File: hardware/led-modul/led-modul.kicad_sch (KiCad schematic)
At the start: 123 parts, among them J201 24V IN 20A, J202 BLOKK 1, J203 BLOKK 2, J204 BLOKK 3, Q201 NTMFS5C604NL, Q202 NTD5C648NL, Q203 NTD5C648NL, Q204 NTD5C648NL, Q205 NTD5C648NL, Q206 NTD5C648NL, Q207 NTD5C648NL, U201 UCC27524DR, U202 UCC27524DR, U203 UCC27524DR, U204 LM74700-Q1, U205 MC78L12ACDR2G, U206 INA181A2IDBVR

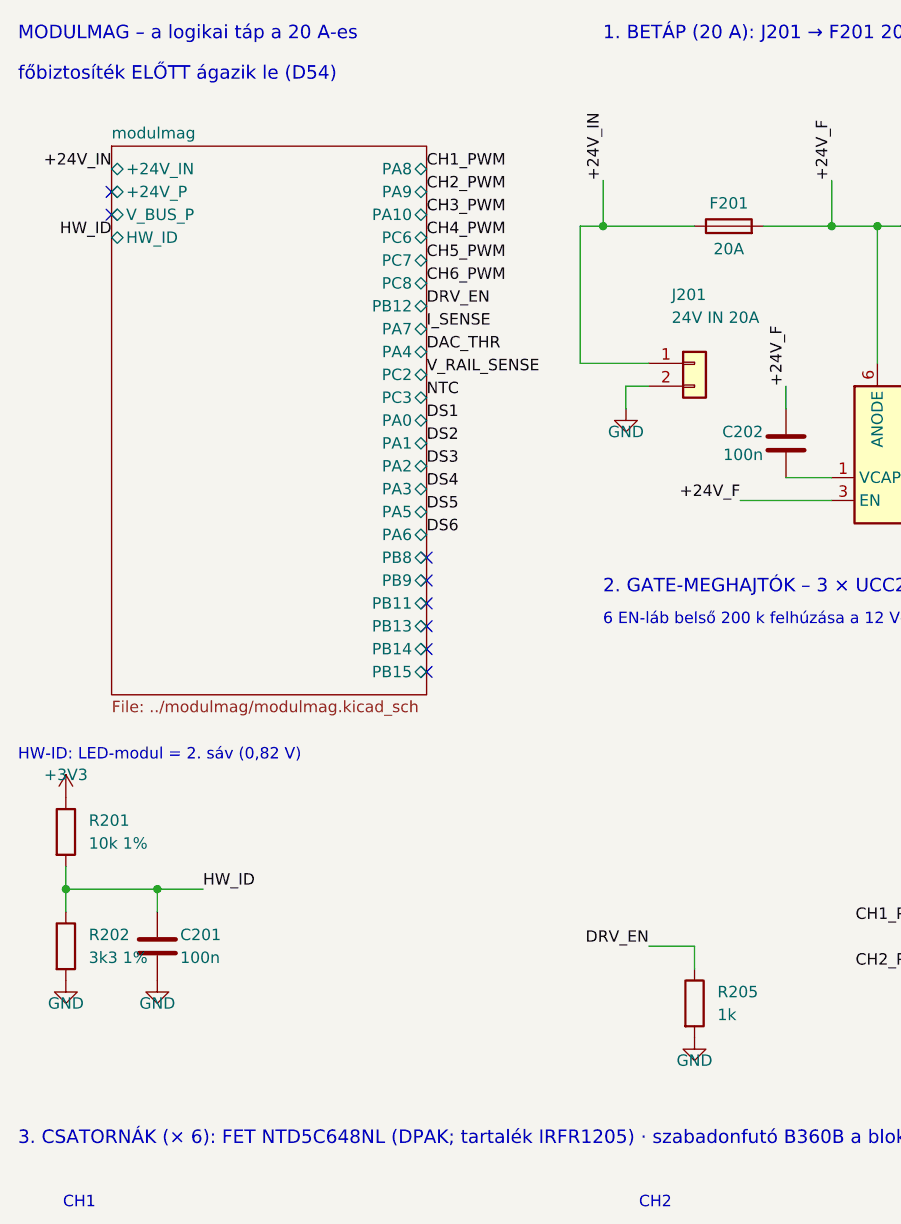
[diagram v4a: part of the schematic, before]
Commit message: Hardver: központi 5 V, közös föld, 12–26 V, HW-ID 16 sáv (D71)
Vezérlő: LMR33630 (5,2 V) + LM66200 (USB-vel VAGY-olva) + TPS259531 eFuse (2 A);
F1 2 A, D1 B360 a 12 V-os működéshez. Modulmag: táp a buszról (AP2112K), TCAN1044AV,
nincs izoláció, PC1 = VBUS_SENSE. LED/relé: VIN_SENSE a PB11-en, relémodul saját
tekercs-táppal. Bemeneti modul: nincs 24 V. HW-ID/HW_REV 16 sáv. Specifikációk,
áttekintés, beszerzés, ütemterv frissítve.

Co-Authored-By: Claude Opus 5.5 <noreply@anthropic.com>
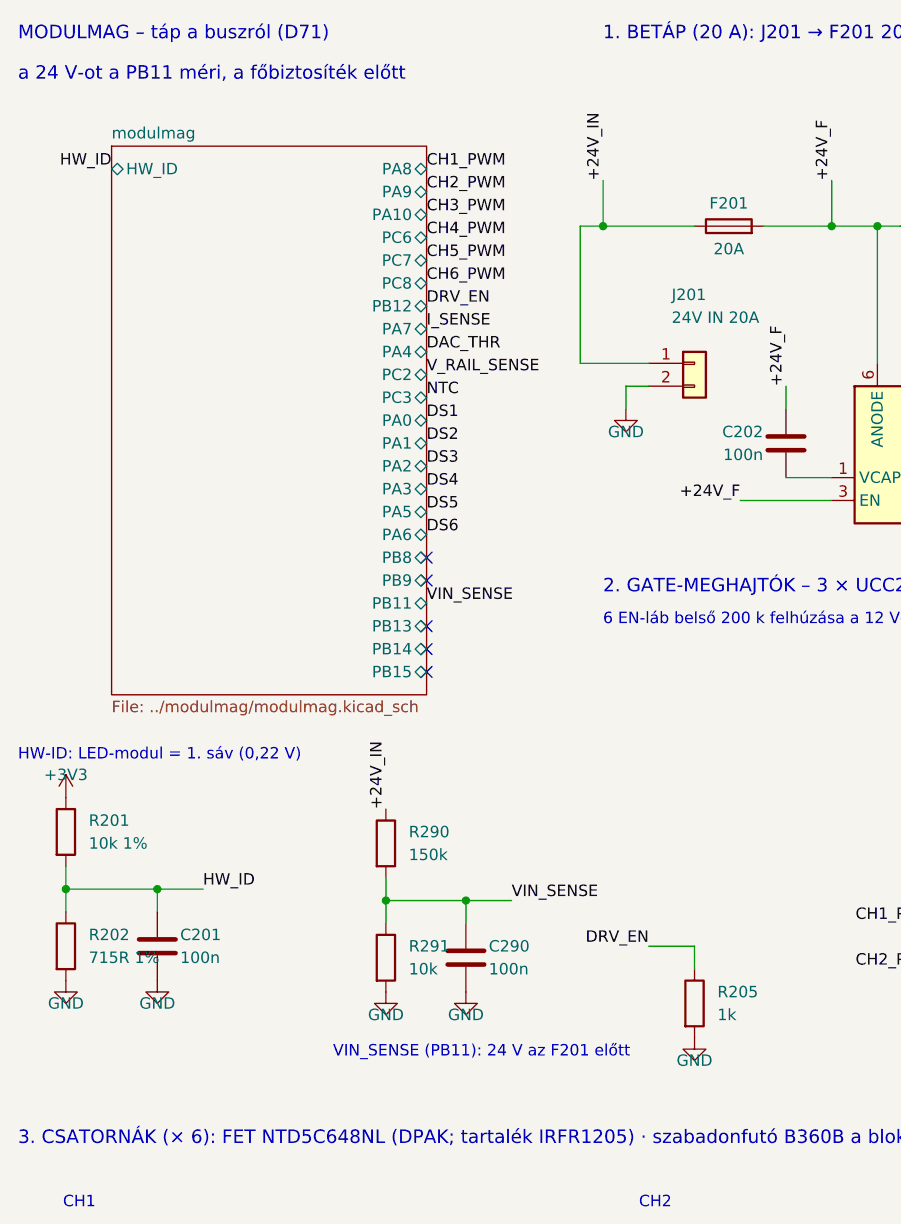
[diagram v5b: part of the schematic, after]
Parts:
- added C290: 100n, Capacitor_SMD:C_0603_1608Metric, symbol Device:C
- added R290: 150k, Resistor_SMD:R_0603_1608Metric, symbol Device:R
- added R291: 10k, Resistor_SMD:R_0603_1608Metric, symbol Device:R
- R202: value 3k3 1% -> 715R 1%
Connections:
- net +24V_IN: now also R290.1
- net GND: now also C290.2, R291.2
- new net VIN_SENSE: C290.1, R290.2, R291.1
- no-connect marks 10 -> 7
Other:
- sheet modulmag ports: added none; removed +24V_IN, +24V_P, V_BUS_P
- note added: "HW-ID: LED-modul = 1. sáv (0,22 V)"
- note added: "MODULMAG – táp a buszról (D71)"
- note added: "VIN_SENSE (PB11): 24 V az F201 előtt"
- note added: "a 24 V-ot a PB11 méri, a főbiztosíték előtt"
- note removed: "HW-ID: LED-modul = 2. sáv (0,82 V)"
- note removed: "MODULMAG – a logikai táp a 20 A-es"
- note removed: "főbiztosíték ELŐTT ágazik le (D54)"

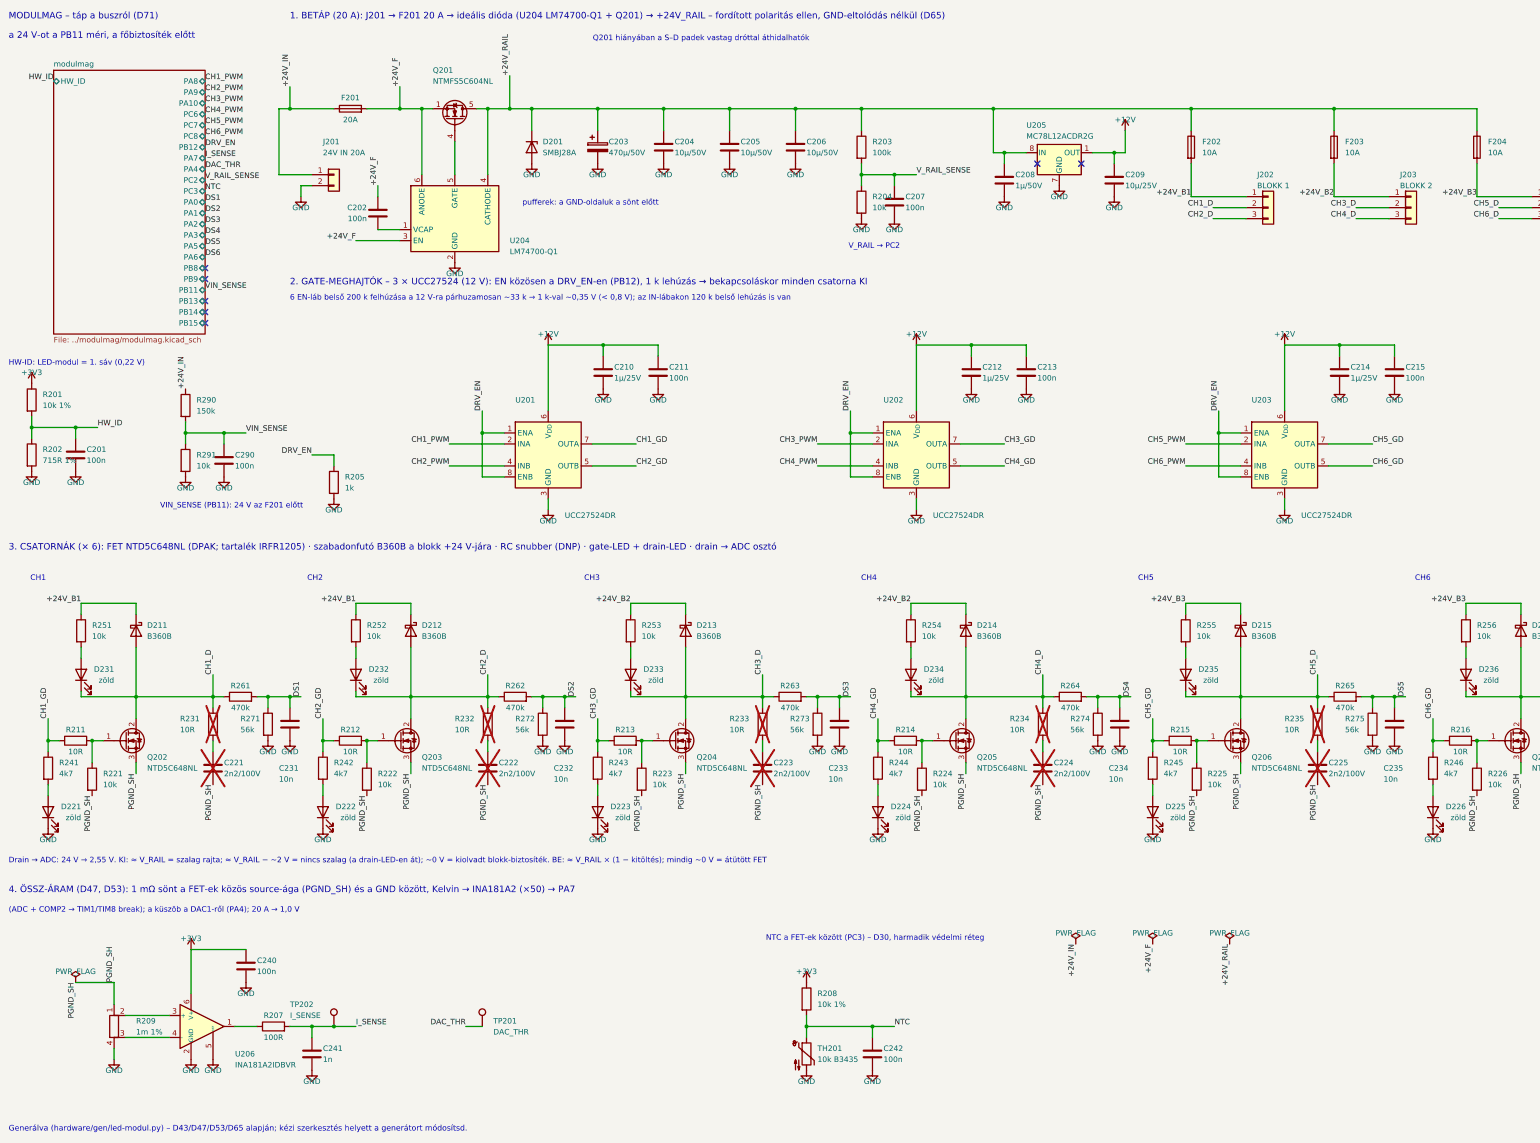
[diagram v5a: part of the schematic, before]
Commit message: Hardver: szakértői javítások (D74–D77), STM32L433 + SN65HVD230 + GND-ági polaritásvédelem (D78–D81), teljes ellenőrzés
- D74–D77: busz-GND ellenállás, CAN-fojtó-hely, TVS a +5V_BUCK-on és a VUSB-n, bemenetvédelem,
  230 V-os és antenna-tiltás a NYÁK-on, SCT-jack footprint
- D78–D80: modul-MCU STM32L433RCT3 (VIN_SENSE PB1, LED: TIM15/TIM16, I_SENSE PA3), modul-transceiver
  SN65HVD230, N-FET a GND-ágban (vezérlő Q1, LED Q201, relé Q100), MCP9701A, táp-LED a +5V-ról,
  2 oz a LED-/relémodulon, AP2112K marad; D81 javaslat (TPD4E02B04 a bemeneteken)
- CubeMX-projektek L433-ra, fejsoros kódgenerálással ellenőrizve (minden periféria inicializálódik)
- gen/ellenorzes.py (ERC, láb ↔ pad, modulmag, CubeMX, polaritásvédelem, NYÁK ↔ rajz, DRC) – 0 hiba
- gen/bom.sh + bom/*.csv darabjegyzék; docs/komponenslista.md a konzulensnek
- kontextus: DONTESEK D74–D81, specifikációk, ATTEKINTES, NAPLO, beszerzési lista; alkatrészkészlet-jegyzet (claude.ai)

Co-Authored-By: Claude Opus 5.5 <noreply@anthropic.com>
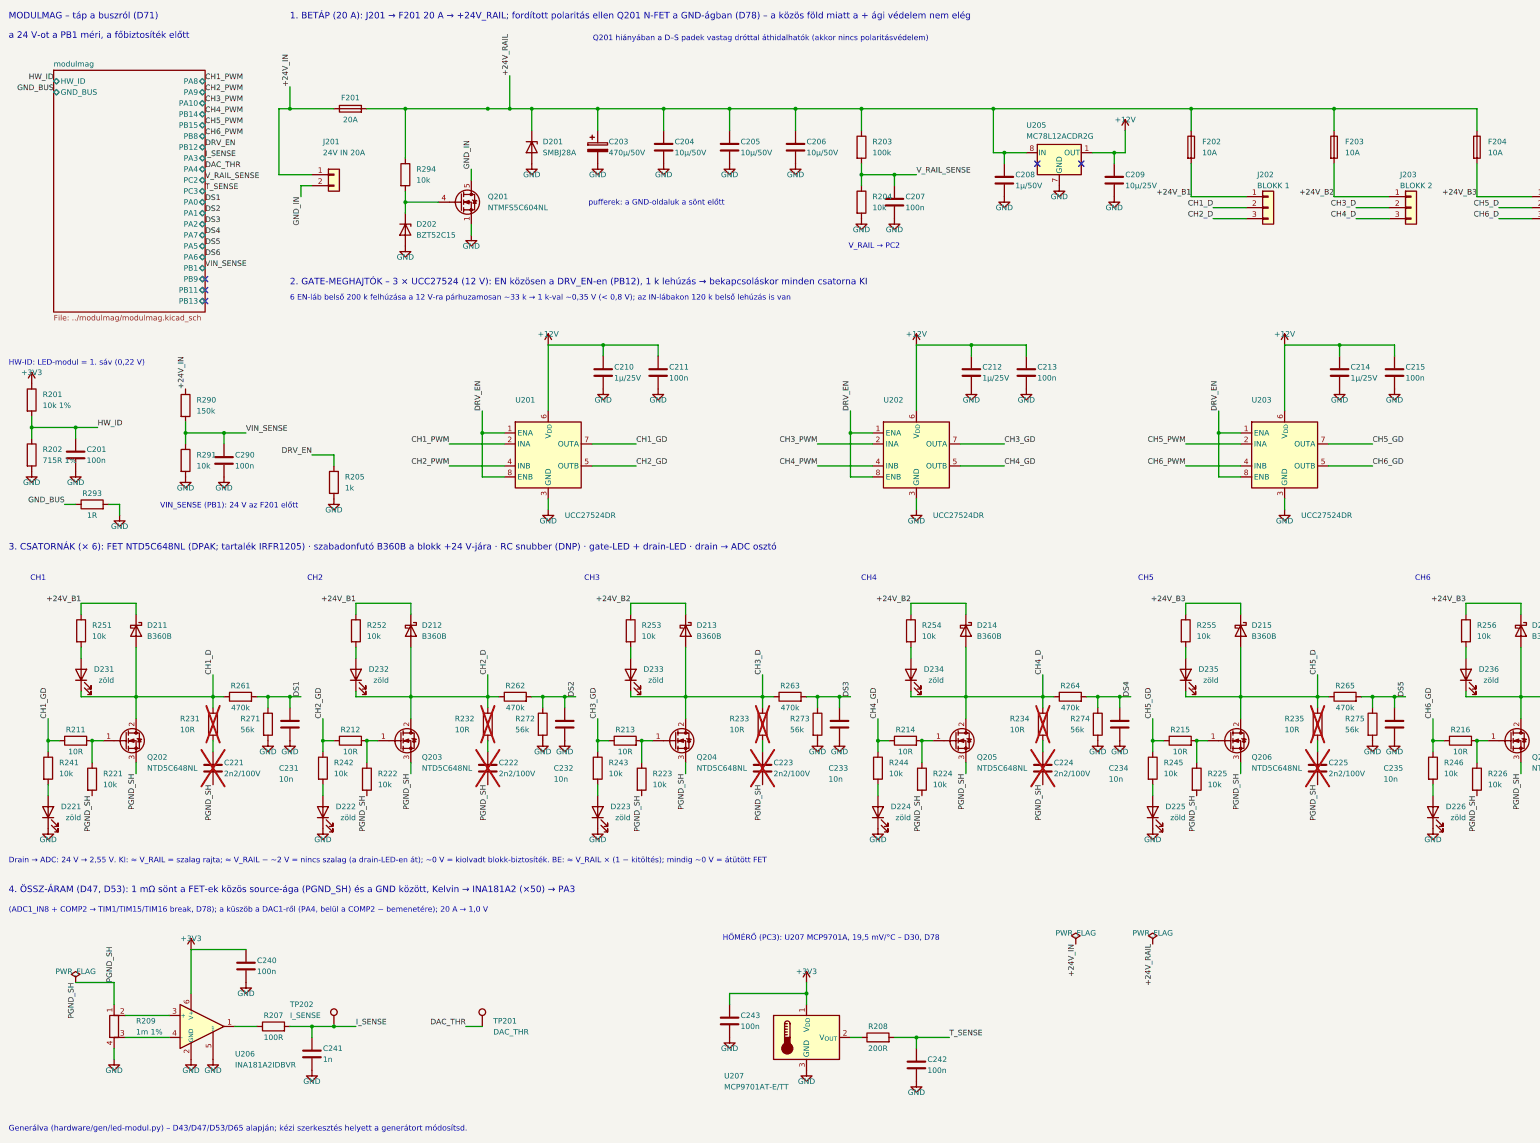
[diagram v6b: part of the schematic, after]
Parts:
- removed C202: 100n, Capacitor_SMD:C_0603_1608Metric, symbol Device:C
- removed TH201: 10k B3435, Resistor_SMD:R_0603_1608Metric, symbol Device:Thermistor_NTC
- removed U204: LM74700-Q1, Package_TO_SOT_SMD:SOT-23-6, symbol Power_Management:LM74700
- added C243: 100n, Capacitor_SMD:C_0603_1608Metric, symbol Device:C
- added D202: BZT52C15, Diode_SMD:D_SOD-123, symbol Device:D_Zener
- added R293: 1R, Resistor_SMD:R_1206_3216Metric, symbol Device:R
- added R294: 10k, Resistor_SMD:R_0603_1608Metric, symbol Device:R
- added U207: MCP9701AT-E/TT, Package_TO_SOT_SMD:SOT-23, symbol Sensor_Temperature:MCP9700Ax-ETT
- F202, F203, F204: Megjegyzés Littelfuse 451/453 NANO² (2410), pl. 0451010.MRL – értéke a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 -> Littelfuse 451/453 NANO² (2410) – értéke a bekötött szalag 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
- J201: Megjegyzés push-in, 2,5 mm², ≥ 20 A – helyőrző; barna = +24 V, kék = G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 -> csavaros (Phoenix MKDS 3, 5,08 mm, 24 A / 4 mm²) – D79; bar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
- J202: Megjegyzés 1 = +24 V, 2 = CH1, 3 = CH2; push-in, ≥ 10 A/pólus – helyőr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 -> 1 = +24 V, 2 = CH1, 3 = CH2; csavaros (MKDS 3, 5,08 mm) – D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
- J203: Megjegyzés 1 = +24 V, 2 = CH3, 3 = CH4; push-in, ≥ 10 A/pólus – helyőr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 -> 1 = +24 V, 2 = CH3, 3 = CH4; csavaros (MKDS 3, 5,08 mm) – D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
- J204: Megjegyzés 1 = +24 V, 2 = CH5, 3 = CH6; push-in, ≥ 10 A/pólus – helyőr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 -> 1 = +24 V, 2 = CH5, 3 = CH6; csavaros (MKDS 3, 5,08 mm) – D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
- Q201: Megjegyzés onsemi 60 V, ~1,2 mΩ, SO-8FL; S = bemenet, D = sín; nagy pa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 -> onsemi 60 V, ~1,2 mΩ, SO-8FL; D = GND_IN (J201), S = GND; n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
- R208: value 10k 1% -> 200R; Megjegyzés (none) -> a VOUT nagy kapacitív terhelés esetén soros ellenállást kér
- R241, R242, R243, R244, R245, R246: value 4k7 -> 10k
- R290: Megjegyzés fordított polaritásnál ~0,16 mA folyik a PB11 védődiódáján 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 -> fordított polaritásnál a Q201 zár, a lap nem kap feszültség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
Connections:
- net +24V_RAIL: now also F201.2, R294.1; no longer Q201.5 (D)
- net +3V3: now also C243.1, U207.1 (V_{DD}); no longer R208.1
- net GND: now also Q201.1 (S), Q201.2 (S), Q201.3 (S), C243.2, D202.2 (A), R293.2, U207.3 (GND); no longer J201.2 (Pin_2)
- net at Q201.4 (G): now also D202.1 (K), R294.2
- removed net +24V_F: F201.2, Q201.1 (S), Q201.2 (S), Q201.3 (S)
- net NTC renamed T_SENSE
- new net: R208.1, U207.2 (V_{OUT})
- new net GND_BUS: R293.1
- new net GND_IN: J201.2 (Pin_2), Q201.5 (D)
- no-connect marks 7 -> 5
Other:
- sheet modulmag ports: added GND_BUS, PB1; removed PC6, PC7, PC8
- note added: "(ADC1_IN8 + COMP2 → TIM1/TIM15/TIM16 break, D78); a küszöb a DAC1-ről (PA4, belül a COMP2 − bemenetére); 20 A → 1,0 V"
- note added: "1. BETÁP (20 A): J201 → F201 20 A → +24V_RAIL; fordított polaritás ellen Q201 N-FET a GND-ágban (D78) – a közös föld miatt a + ági védelem nem elég"
- note added: "4. ÖSSZ-ÁRAM (D47, D53): 1 mΩ sönt a FET-ek közös source-ága (PGND_SH) és a GND között, Kelvin → INA181A2 (×50) → PA3"
- note added: "HŐMÉRŐ (PC3): U207 MCP9701A, 19,5 mV/°C – D30, D78"
- note added: "Q201 hiányában a D–S padek vastag dróttal áthidalhatók (akkor nincs polaritásvédelem)"
- note added: "VIN_SENSE (PB1): 24 V az F201 előtt"
- note added: "a 24 V-ot a PB1 méri, a főbiztosíték előtt"
- note removed: "(ADC + COMP2 → TIM1/TIM8 break); a küszöb a DAC1-ről (PA4); 20 A → 1,0 V"
- note removed: "1. BETÁP (20 A): J201 → F201 20 A → ideális dióda (U204 LM74700-Q1 + Q201) → +24V_RAIL – fordított polaritás ellen, GND-eltolódás nélkül (D65)"
- note removed: "4. ÖSSZ-ÁRAM (D47, D53): 1 mΩ sönt a FET-ek közös source-ága (PGND_SH) és a GND között, Kelvin → INA181A2 (×50) → PA7"
- note removed: "NTC a FET-ek között (PC3) – D30, harmadik védelmi réteg"
- note removed: "Q201 hiányában a S–D padek vastag dróttal áthidalhatók"
- note removed: "VIN_SENSE (PB11): 24 V az F201 előtt"
- note removed: "a 24 V-ot a PB11 méri, a főbiztosíték előtt"
